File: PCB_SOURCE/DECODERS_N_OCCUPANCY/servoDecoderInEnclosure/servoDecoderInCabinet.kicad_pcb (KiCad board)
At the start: 2 copper layers, 75 x 84 mm, 110 parts, among them J101 Screw_Terminal_01x04, J201 ICSP, J702 USB_B_Mini, U1001 6N137, U202 ATmega328-A, U301 L78L05_SOT89, U701 CH340G, Y201 Crystal_GND2, Y701 Crystal

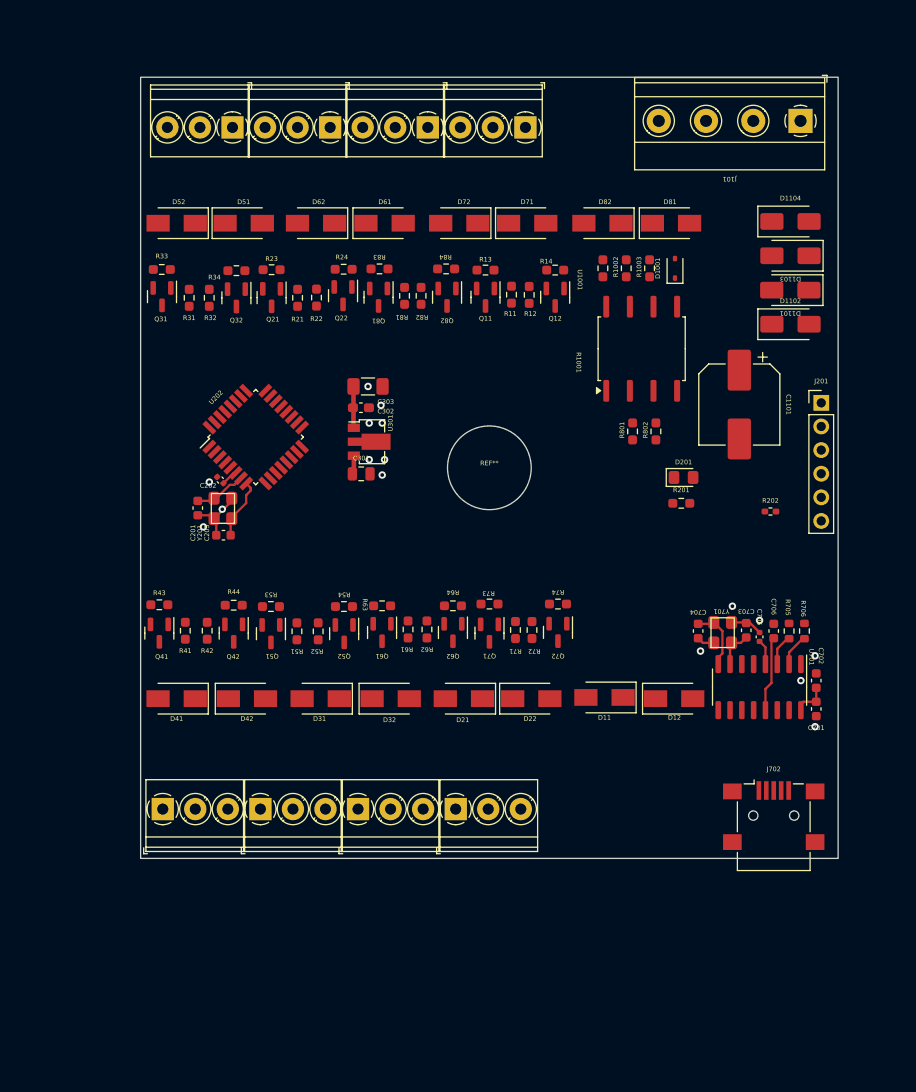
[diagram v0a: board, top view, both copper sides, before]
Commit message: added some boards, new turning loop module with sleeper, all eating LED as well as servoDecoderInEnclosure
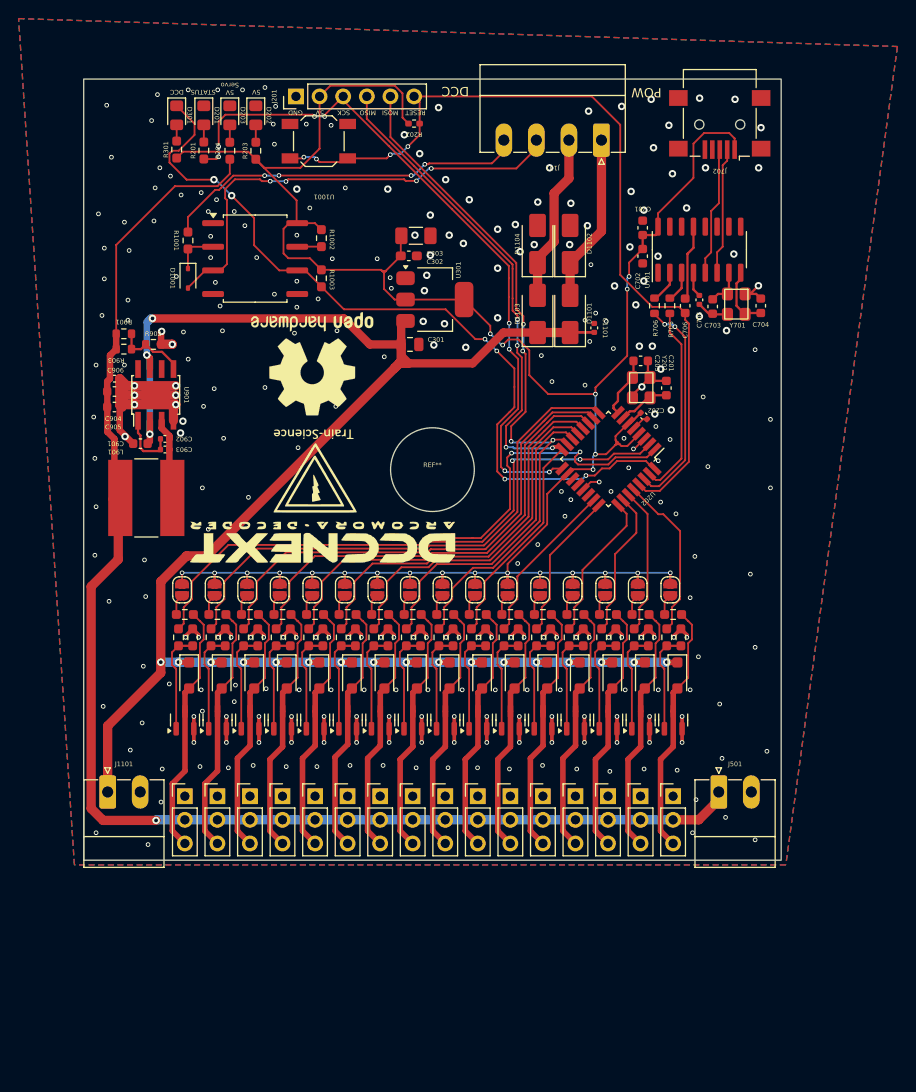
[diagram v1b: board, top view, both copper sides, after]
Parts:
- removed D11, D12, D21, D22, D31, D32, D41, D42, D51, D52, D61, D62, D71, D72, D81, D82: ~, Diode_SMD:D_SMA
- removed Q11, Q12, Q21, Q22, Q31, Q32, Q41, Q42, Q51, Q52, Q61, Q62, Q71, Q72, Q81, Q82: ~, Package_TO_SOT_SMD:SOT-23
- removed R11, R12, R13, R14, R21, R22, R23, R24, R31, R32, R33, R34, R41, R42, R43, R44, R51, R52, R53, R54, R61, R62, R63, R64, R71, R72, R73, R74, R81, R82, R83, R84: ~, Resistor_SMD:R_0603_1608Metric_Pad0.98x0.95mm_HandSolder
- removed the REF** at (218.0, 46.2)
- removed the REF** at (197.0, 46.2)
- removed the REF** at (210.5, 119.5)
- removed the REF** at (207.5, 46.2)
- removed the REF** at (189.5, 119.5)
- removed the REF** at (200.0, 119.5)
- removed the REF** at (186.5, 46.2)
- removed the REF** at (179.0, 119.5)
- added C901: 22uF, Capacitor_SMD:C_0603_1608Metric, F.Cu at (176.6, 80.2)
- added C902: 100nF, Capacitor_SMD:C_0402_1005Metric, F.Cu at (179.2, 79.7)
- added C903: 22nF, Capacitor_SMD:C_0402_1005Metric, F.Cu at (179.2, 80.8)
- added C904: 22uF, Capacitor_SMD:C_0603_1608Metric, F.Cu at (173.8, 74.6)
- added C905: 22uF, Capacitor_SMD:C_0603_1608Metric, F.Cu at (173.8, 76.3)
- added C906: 100nF, Capacitor_SMD:C_0402_1005Metric, F.Cu at (173.8, 73.2)
- added D1002: SM4007, Diode_SMD:D_SOD-123F, F.Cu at (195.8, 105.1)
- added D1301: SM4007, Diode_SMD:D_SOD-123F, F.Cu at (199.3, 105.1)
- added D1401: SM4007, Diode_SMD:D_SOD-123F, F.Cu at (202.8, 105.1)
- added D1501: SM4007, Diode_SMD:D_SOD-123F, F.Cu at (206.3, 105.1)
- added D1601: SM4007, Diode_SMD:D_SOD-123F, F.Cu at (209.8, 105.1)
- added D1701: SM4007, Diode_SMD:D_SOD-123F, F.Cu at (213.3, 105.1)
- added D1801: SM4007, Diode_SMD:D_SOD-123F, F.Cu at (216.8, 105.1)
- added D1901: SM4007, Diode_SMD:D_SOD-123F, F.Cu at (220.3, 105.1)
- added D2001: SM4007, Diode_SMD:D_SOD-123F, F.Cu at (223.8, 105.1)
- added D202: LED, LED_SMD:LED_0805_2012Metric_Pad1.15x1.40mm_HandSolder, F.Cu at (189.0, 44.9)
- added D203: LED, LED_SMD:LED_0805_2012Metric_Pad1.15x1.40mm_HandSolder, F.Cu at (186.2, 44.9)
- added D2101: SM4007, Diode_SMD:D_SOD-123F, F.Cu at (227.3, 105.1)
- added D2201: SM4007, Diode_SMD:D_SOD-123F, F.Cu at (230.8, 105.1)
- added D2301: SM4007, Diode_SMD:D_SOD-123F, F.Cu at (234.3, 105.1)
- added D301: LED, LED_SMD:LED_0805_2012Metric_Pad1.15x1.40mm_HandSolder, F.Cu at (180.5, 44.9)
- added D601: SM4007, Diode_SMD:D_SOD-123F, F.Cu at (185.3, 105.1)
- added D701: SM4007, Diode_SMD:D_SOD-123F, F.Cu at (188.8, 105.1)
- added D801: SM4007, Diode_SMD:D_SOD-123F, F.Cu at (181.8, 105.1)
- added D901: SM4007, Diode_SMD:D_SOD-123F, F.Cu at (192.3, 105.1)
- added G***: LOGO, custom_kicad_lib_sk:Train-Science logo small, F.Cu at (195.3, 83.1)
- added G***: LOGO, custom_kicad_lib_sk:DCC_NEXT_LOGO, F.Cu at (196.2, 90.6)
- added J1001: Conn_01x03_Pin, Connector_PinHeader_2.54mm:PinHeader_1x03_P2.54mm_Vertical, F.Cu at (195.4, 118.1)
- added J1101: Screw_Terminal_01x02, Connector_Phoenix_MC:PhoenixContact_MC_1,5_2-G-3.5_1x02_P3.50mm_Horizontal, F.Cu at (173.1, 117.7)
- added J1301: Conn_01x03_Pin, Connector_PinHeader_2.54mm:PinHeader_1x03_P2.54mm_Vertical, F.Cu at (198.9, 118.1)
- added J1401: Conn_01x03_Pin, Connector_PinHeader_2.54mm:PinHeader_1x03_P2.54mm_Vertical, F.Cu at (202.4, 118.1)
- added J1501: Conn_01x03_Pin, Connector_PinHeader_2.54mm:PinHeader_1x03_P2.54mm_Vertical, F.Cu at (205.9, 118.1)
- added J1601: Conn_01x03_Pin, Connector_PinHeader_2.54mm:PinHeader_1x03_P2.54mm_Vertical, F.Cu at (209.4, 118.1)
- added J1701: Conn_01x03_Pin, Connector_PinHeader_2.54mm:PinHeader_1x03_P2.54mm_Vertical, F.Cu at (212.9, 118.1)
- added J1801: Conn_01x03_Pin, Connector_PinHeader_2.54mm:PinHeader_1x03_P2.54mm_Vertical, F.Cu at (216.4, 118.1)
- added J1901: Conn_01x03_Pin, Connector_PinHeader_2.54mm:PinHeader_1x03_P2.54mm_Vertical, F.Cu at (219.9, 118.1)
- added J2001: Conn_01x03_Pin, Connector_PinHeader_2.54mm:PinHeader_1x03_P2.54mm_Vertical, F.Cu at (223.4, 118.1)
- added J2101: Conn_01x03_Pin, Connector_PinHeader_2.54mm:PinHeader_1x03_P2.54mm_Vertical, F.Cu at (226.9, 118.1)
- added J2201: Conn_01x03_Pin, Connector_PinHeader_2.54mm:PinHeader_1x03_P2.54mm_Vertical, F.Cu at (230.4, 118.1)
- added J2301: Conn_01x03_Pin, Connector_PinHeader_2.54mm:PinHeader_1x03_P2.54mm_Vertical, F.Cu at (233.9, 118.1)
- added J501: Screw_Terminal_01x02, Connector_Phoenix_MC:PhoenixContact_MC_1,5_2-G-3.5_1x02_P3.50mm_Horizontal, F.Cu at (238.8, 117.7)
- added J601: Conn_01x03_Pin, Connector_PinHeader_2.54mm:PinHeader_1x03_P2.54mm_Vertical, F.Cu at (184.9, 118.1)
- added J701: Conn_01x03_Pin, Connector_PinHeader_2.54mm:PinHeader_1x03_P2.54mm_Vertical, F.Cu at (188.4, 118.1)
- added J801: Conn_01x03_Pin, Connector_PinHeader_2.54mm:PinHeader_1x03_P2.54mm_Vertical, F.Cu at (181.4, 118.1)
- added J901: Conn_01x03_Pin, Connector_PinHeader_2.54mm:PinHeader_1x03_P2.54mm_Vertical, F.Cu at (191.9, 118.1)
- added JP1001: SolderJumper_2_Open, Jumper:SolderJumper-2_P1.3mm_Open_RoundedPad1.0x1.5mm, F.Cu at (195.1, 95.9)
- added JP1301: SolderJumper_2_Open, Jumper:SolderJumper-2_P1.3mm_Open_RoundedPad1.0x1.5mm, F.Cu at (198.6, 95.9)
- added JP1401: SolderJumper_2_Open, Jumper:SolderJumper-2_P1.3mm_Open_RoundedPad1.0x1.5mm, F.Cu at (202.1, 95.9)
- added JP1501: SolderJumper_2_Open, Jumper:SolderJumper-2_P1.3mm_Open_RoundedPad1.0x1.5mm, F.Cu at (205.6, 95.9)
- added JP1601: SolderJumper_2_Open, Jumper:SolderJumper-2_P1.3mm_Open_RoundedPad1.0x1.5mm, F.Cu at (209.1, 95.9)
- added JP1701: SolderJumper_2_Open, Jumper:SolderJumper-2_P1.3mm_Open_RoundedPad1.0x1.5mm, F.Cu at (212.6, 95.9)
- added JP1801: SolderJumper_2_Open, Jumper:SolderJumper-2_P1.3mm_Open_RoundedPad1.0x1.5mm, F.Cu at (216.1, 95.9)
- added JP1901: SolderJumper_2_Open, Jumper:SolderJumper-2_P1.3mm_Open_RoundedPad1.0x1.5mm, F.Cu at (219.6, 95.9)
- added JP2001: SolderJumper_2_Open, Jumper:SolderJumper-2_P1.3mm_Open_RoundedPad1.0x1.5mm, F.Cu at (223.1, 95.9)
- added JP2101: SolderJumper_2_Open, Jumper:SolderJumper-2_P1.3mm_Open_RoundedPad1.0x1.5mm, F.Cu at (226.6, 95.9)
- added JP2201: SolderJumper_2_Open, Jumper:SolderJumper-2_P1.3mm_Open_RoundedPad1.0x1.5mm, F.Cu at (230.1, 95.9)
- added JP2301: SolderJumper_2_Open, Jumper:SolderJumper-2_P1.3mm_Open_RoundedPad1.0x1.5mm, F.Cu at (233.6, 95.9)
- added JP601: SolderJumper_2_Open, Jumper:SolderJumper-2_P1.3mm_Open_RoundedPad1.0x1.5mm, F.Cu at (184.6, 95.9)
- added JP701: SolderJumper_2_Open, Jumper:SolderJumper-2_P1.3mm_Open_RoundedPad1.0x1.5mm, F.Cu at (188.1, 95.9)
- added JP801: SolderJumper_2_Open, Jumper:SolderJumper-2_P1.3mm_Open_RoundedPad1.0x1.5mm, F.Cu at (181.1, 95.9)
- added JP901: SolderJumper_2_Open, Jumper:SolderJumper-2_P1.3mm_Open_RoundedPad1.0x1.5mm, F.Cu at (191.6, 95.9)
- added L901: L, Inductor_SMD:L_Bourns-SRN8040_8x8.15mm, F.Cu at (177.2, 86.0)
- added Q1001: AO3400A, Package_TO_SOT_SMD:SOT-23, F.Cu at (195.4, 109.9)
- added Q1301: AO3400A, Package_TO_SOT_SMD:SOT-23, F.Cu at (198.9, 109.9)
- added Q1401: AO3400A, Package_TO_SOT_SMD:SOT-23, F.Cu at (202.4, 109.9)
- added Q1501: AO3400A, Package_TO_SOT_SMD:SOT-23, F.Cu at (205.9, 109.9)
- added Q1601: AO3400A, Package_TO_SOT_SMD:SOT-23, F.Cu at (209.4, 109.9)
- added Q1701: AO3400A, Package_TO_SOT_SMD:SOT-23, F.Cu at (212.9, 109.9)
- added Q1801: AO3400A, Package_TO_SOT_SMD:SOT-23, F.Cu at (216.4, 109.9)
- added Q1901: AO3400A, Package_TO_SOT_SMD:SOT-23, F.Cu at (219.9, 109.9)
- added Q2001: AO3400A, Package_TO_SOT_SMD:SOT-23, F.Cu at (223.4, 109.9)
- added Q2101: AO3400A, Package_TO_SOT_SMD:SOT-23, F.Cu at (226.9, 109.9)
- added Q2201: AO3400A, Package_TO_SOT_SMD:SOT-23, F.Cu at (230.4, 109.9)
- added Q2301: AO3400A, Package_TO_SOT_SMD:SOT-23, F.Cu at (233.9, 109.9)
- added Q601: AO3400A, Package_TO_SOT_SMD:SOT-23, F.Cu at (184.9, 109.9)
- added Q701: AO3400A, Package_TO_SOT_SMD:SOT-23, F.Cu at (188.4, 109.9)
- added Q801: AO3400A, Package_TO_SOT_SMD:SOT-23, F.Cu at (181.4, 109.9)
- added Q901: AO3400A, Package_TO_SOT_SMD:SOT-23, F.Cu at (191.9, 109.9)
- added R1004: 22R, custom_kicad_lib_sk:R_0603_smalltext, F.Cu at (194.7, 101.0)
- added R1005: 22k, custom_kicad_lib_sk:R_0603_smalltext, F.Cu at (196.2, 101.0)
- added R1006: 10k, custom_kicad_lib_sk:R_0603_smalltext, F.Cu at (195.4, 98.6)
- added R1301: 22R, custom_kicad_lib_sk:R_0603_smalltext, F.Cu at (198.2, 101.0)
- added R1302: 22k, custom_kicad_lib_sk:R_0603_smalltext, F.Cu at (199.7, 101.0)
- added R1303: 10k, custom_kicad_lib_sk:R_0603_smalltext, F.Cu at (198.9, 98.6)
- added R1401: 22R, custom_kicad_lib_sk:R_0603_smalltext, F.Cu at (201.7, 101.0)
- added R1402: 22k, custom_kicad_lib_sk:R_0603_smalltext, F.Cu at (203.2, 101.0)
- added R1403: 10k, custom_kicad_lib_sk:R_0603_smalltext, F.Cu at (202.4, 98.6)
- added R1501: 22R, custom_kicad_lib_sk:R_0603_smalltext, F.Cu at (205.2, 101.0)
- added R1502: 22k, custom_kicad_lib_sk:R_0603_smalltext, F.Cu at (206.7, 101.0)
- added R1503: 10k, custom_kicad_lib_sk:R_0603_smalltext, F.Cu at (205.9, 98.6)
- added R1601: 22R, custom_kicad_lib_sk:R_0603_smalltext, F.Cu at (208.7, 101.0)
- added R1602: 22k, custom_kicad_lib_sk:R_0603_smalltext, F.Cu at (210.2, 101.0)
- added R1603: 10k, custom_kicad_lib_sk:R_0603_smalltext, F.Cu at (209.4, 98.6)
- added R1701: 22R, custom_kicad_lib_sk:R_0603_smalltext, F.Cu at (212.2, 101.0)
- added R1702: 22k, custom_kicad_lib_sk:R_0603_smalltext, F.Cu at (213.7, 101.0)
- added R1703: 10k, custom_kicad_lib_sk:R_0603_smalltext, F.Cu at (212.9, 98.6)
- added R1801: 22R, custom_kicad_lib_sk:R_0603_smalltext, F.Cu at (215.7, 101.0)
- added R1802: 22k, custom_kicad_lib_sk:R_0603_smalltext, F.Cu at (217.2, 101.0)
- added R1803: 10k, custom_kicad_lib_sk:R_0603_smalltext, F.Cu at (216.4, 98.6)
- added R1901: 22R, custom_kicad_lib_sk:R_0603_smalltext, F.Cu at (219.2, 101.0)
- added R1902: 22k, custom_kicad_lib_sk:R_0603_smalltext, F.Cu at (220.7, 101.0)
- added R1903: 10k, custom_kicad_lib_sk:R_0603_smalltext, F.Cu at (219.9, 98.6)
- added R2001: 22R, custom_kicad_lib_sk:R_0603_smalltext, F.Cu at (222.7, 101.0)
- added R2002: 22k, custom_kicad_lib_sk:R_0603_smalltext, F.Cu at (224.2, 101.0)
- added R2003: 10k, custom_kicad_lib_sk:R_0603_smalltext, F.Cu at (223.4, 98.6)
- added R203: 6k2, Resistor_SMD:R_0603_1608Metric_Pad0.98x0.95mm_HandSolder, F.Cu at (189.0, 48.7)
- added R204: 6k2, Resistor_SMD:R_0603_1608Metric_Pad0.98x0.95mm_HandSolder, F.Cu at (186.2, 48.7)
- added R2101: 22R, custom_kicad_lib_sk:R_0603_smalltext, F.Cu at (226.2, 101.0)
- added R2102: 22k, custom_kicad_lib_sk:R_0603_smalltext, F.Cu at (227.7, 101.0)
- added R2103: 10k, custom_kicad_lib_sk:R_0603_smalltext, F.Cu at (226.9, 98.6)
- added R2201: 22R, custom_kicad_lib_sk:R_0603_smalltext, F.Cu at (229.7, 101.0)
- added R2202: 22k, custom_kicad_lib_sk:R_0603_smalltext, F.Cu at (231.2, 101.0)
- added R2203: 10k, custom_kicad_lib_sk:R_0603_smalltext, F.Cu at (230.4, 98.6)
- added R2301: 22R, custom_kicad_lib_sk:R_0603_smalltext, F.Cu at (233.2, 101.0)
- added R2302: 22k, custom_kicad_lib_sk:R_0603_smalltext, F.Cu at (234.7, 101.0)
- added R2303: 10k, custom_kicad_lib_sk:R_0603_smalltext, F.Cu at (233.9, 98.6)
- added R301: 6k2, Resistor_SMD:R_0603_1608Metric_Pad0.98x0.95mm_HandSolder, F.Cu at (180.5, 48.6)
- added R601: 22R, custom_kicad_lib_sk:R_0603_smalltext, F.Cu at (184.2, 101.0)
- added R602: 22k, custom_kicad_lib_sk:R_0603_smalltext, F.Cu at (185.7, 101.0)
- added R603: 10k, custom_kicad_lib_sk:R_0603_smalltext, F.Cu at (184.9, 98.6)
- added R701: 22R, custom_kicad_lib_sk:R_0603_smalltext, F.Cu at (187.7, 101.0)
- added R702: 22k, custom_kicad_lib_sk:R_0603_smalltext, F.Cu at (189.2, 101.0)
- added R703: 10k, custom_kicad_lib_sk:R_0603_smalltext, F.Cu at (188.4, 98.6)
- added R803: 10k, custom_kicad_lib_sk:R_0603_smalltext, F.Cu at (181.4, 98.6)
- added R901: 220k, Resistor_SMD:R_0603_1608Metric, F.Cu at (174.8, 68.4)
- added R902: 20k, Resistor_SMD:R_0603_1608Metric, F.Cu at (178.0, 69.5)
- added R903: 150k, Resistor_SMD:R_0603_1608Metric, F.Cu at (174.8, 70.0)
- added R904: 22R, custom_kicad_lib_sk:R_0603_smalltext, F.Cu at (191.2, 101.0)
- added R905: 22k, custom_kicad_lib_sk:R_0603_smalltext, F.Cu at (192.7, 101.0)
- added R906: 10k, custom_kicad_lib_sk:R_0603_smalltext, F.Cu at (191.9, 98.6)
- added REF**: OSHW-Logo2_14.6x12mm_SilkScreen, Symbol:OSHW-Logo2_14.6x12mm_SilkScreen, F.Cu at (195.1, 71.6)
- added SW201: default_switch, custom_kicad_lib_sk:default_switch, F.Cu at (195.8, 47.7)
- added U901: MT2499A, Package_SO:TI_SO-PowerPAD-8, F.Cu at (178.2, 75.0)
- C1101: value 1000uF -> 100nF; footprint Capacitor_SMD:CP_Elec_8x10.5 -> Capacitor_SMD:C_0402_1005Metric
- J101: value Screw_Terminal_01x04 -> FEMALE; footprint TerminalBlock_Phoenix:TerminalBlock_Phoenix_MKDS-1,5-4-5.08_1x04_P5.08mm_Horizontal -> Connector_Phoenix_MC:PhoenixContact_MC_1,5_4-G-3.5_1x04_P3.50mm_Horizontal
- R801: value 10k -> 22R
- R802: value 10k -> 22k
- U301: value L78L05_SOT89 -> AMS1117-5.0; footprint Package_TO_SOT_SMD:SOT-89-3 -> Package_TO_SOT_SMD:SOT-223-3_TabPin2
- moved J702 74.5 mm to (238.9, 45.9), turned to 180 degrees
- moved J201 65.4 mm to (193.3, 42.9), turned to 90 degrees
- moved D201 64.6 mm to (183.4, 44.9), turned to -90 degrees
- moved R201 63.8 mm to (183.4, 48.7), turned to 90 degrees
- moved R202 56.6 mm to (206.0, 45.8), turned to 180 degrees
- moved C701 55.0 mm to (230.6, 57.0), turned to 90 degrees
- moved R802 54.5 mm to (182.2, 101.0)
- moved R801 53.6 mm to (180.7, 101.0), turned to -90 degrees
- moved D1001 52.4 mm to (181.7, 62.4), turned to -90 degrees
- moved C201 52.0 mm to (233.2, 74.2), turned to -90 degrees
- moved C702 49.3 mm to (230.6, 60.0), turned to -90 degrees
- moved C203 48.6 mm to (230.4, 71.3), turned to 180 degrees
- moved U701 47.5 mm to (236.7, 59.3), turned to 90 degrees
- moved Y201 46.4 mm to (230.2, 74.1), turned to 90 degrees
- moved C202 46.1 mm to (230.7, 77.2), turned to -45 degrees
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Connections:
- net /A renamed /DCC/A
- net /B renamed /DCC/B
- net /atmega/sw3 renamed /atmega/P9
- net /atmega/sw4 renamed /atmega/P10
- C1101 pad 1: /Buck/VCC -> GND
- C1101 pad 2: GND -> VCC
- C301 pad 1: /Buck/VCC -> VCC
- D1101 pad 1: /Buck/VCC -> VCC
- D1101 pad 2: /D_bridge/AC_1 -> /D_bridge/AC_2
- D1102 pad 1: /D_bridge/AC_1 -> /D_bridge/AC_2
- D1103 pad 1: /Buck/VCC -> VCC
- D1103 pad 2: /D_bridge/AC_2 -> /D_bridge/AC_1
- D1104 pad 1: /D_bridge/AC_2 -> /D_bridge/AC_1
- D201 pad 1: /atmega/LED -> GND
- R201 pad 1: +5V -> /atmega/LED
- R801 pad 1: /atmega/bus2.pin1 -> /atmega/P1
- R801 pad 2: +5V -> Net-(Q801-G)
- R802 pad 1: /atmega/bus2.pin2 -> Net-(Q801-G)
- R802 pad 2: +5V -> GND
- U202 pad 1: /atmega/bus1.pin1 -> /atmega/P1
- U202 pad 10: /atmega/bus1.relay2 -> /atmega/P4
- U202 pad 11: /atmega/bus2.pin1 -> /atmega/P5
- U202 pad 12: /atmega/bus2.relay1 -> /atmega/P6
- U202 pad 13: /atmega/sw1 -> /atmega/P7
- U202 pad 14: /atmega/sw2 -> /atmega/P8
- U202 pad 2: /atmega/bus1.pin2 -> /atmega/P2
- U202 pad 23: /atmega/bus2.relay2 -> /atmega/P11
- U202 pad 24: /atmega/bus2.pin2 -> /atmega/P12
- U202 pad 25: /atmega/bus3.pin1 -> /atmega/P13
- U202 pad 26: /atmega/bus3.pin2 -> /atmega/P14
- U202 pad 27: /atmega/bus3.relay1 -> /atmega/P15
- U202 pad 28: /atmega/bus3.relay2 -> /atmega/P16
- U202 pad 9: /atmega/bus1.relay1 -> /atmega/P3
- U301 pad 1: +5V -> GND
- U301 pad 2: GND -> +5V
- U301 pad 3: /Buck/VCC -> VCC
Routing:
- net VCC: track 0.00 -> 262.1 mm, vias 0 -> 20
- net +5V: track 10.1 -> 266.1 mm, vias 0 -> 23
- net +5VA: track 0.00 -> 149.6 mm, vias 0 -> 1
- net GND: track 12.2 -> 134.1 mm, vias 11 -> 288
- net /USB/Reset: track 0.00 -> 91.3 mm, vias 0 -> 4
- net /DCC/DCC_TTL: track 0.00 -> 87.0 mm, vias 0 -> 6
- net /atmega/P9: track 0.00 -> 76.9 mm, vias 0 -> 4
- net /atmega/P10: track 0.00 -> 76.1 mm, vias 0 -> 4
- net /atmega/LED: track 0.00 -> 75.6 mm, vias 0 -> 8
- net /atmega/P1: track 0.00 -> 67.5 mm, vias 0 -> 2
- net /atmega/P2: track 0.00 -> 60.9 mm, vias 0 -> 2
- net /atmega/P3: track 0.00 -> 54.8 mm
- net /atmega/P4: track 0.00 -> 50.6 mm
- net /DCC/B: track 0.00 -> 49.9 mm, vias 0 -> 4
- net /atmega/P5: track 0.00 -> 46.4 mm
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- added copper zone on B.Cu, net GND
- added copper zone on F.Cu, net GND
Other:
- board text added: "5V"
- board text added: "5V Servo"
- board text added: "DCC"
- board text added: "GND"
- board text added: "MISO"
- board text added: "MOSI"
- board text added: "POW"
- board text added: "RESET"
- board text added: "SCK"
- board text added: "STATUS"

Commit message: added S88 current sense to releases and update OSSD decoder
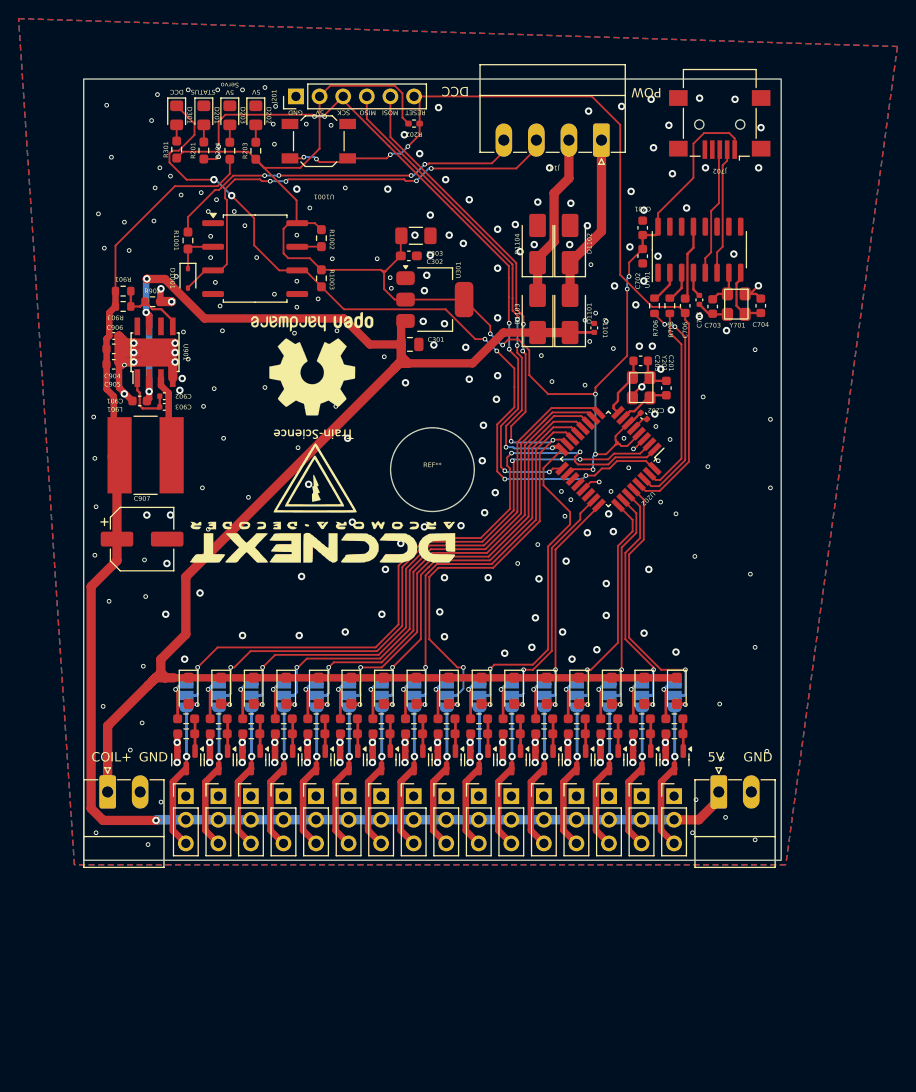
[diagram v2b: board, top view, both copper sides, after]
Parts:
- removed D1002, D1301, D1401, D1501, D1601, D1701, D1801, D1901, D2001, D2201, D2301, D601, D701, D801, D901: SM4007, Diode_SMD:D_SOD-123F
- removed J1001, J1301, J1401, J1501, J1601, J1701, J1801, J1901, J2001, J2201, J2301, J601, J701, J801, J901: Conn_01x03_Pin, Connector_PinHeader_2.54mm:PinHeader_1x03_P2.54mm_Vertical
- removed JP1001, JP1301, JP1401, JP1501, JP1601, JP1701, JP1801, JP1901, JP2001, JP2201, JP2301, JP601, JP701, JP801, JP901: SolderJumper_2_Open, Jumper:SolderJumper-2_P1.3mm_Open_RoundedPad1.0x1.5mm
- removed Q1001, Q1301, Q1401, Q1501, Q1601, Q1701, Q1801, Q1901, Q2001, Q2201, Q2301, Q601, Q701, Q801, Q901: AO3400A, Package_TO_SOT_SMD:SOT-23
- removed R1004, R1301, R1401, R1501, R1601, R1701, R1801, R1901, R2001, R2201, R2301, R601, R701, R801, R904: 22R, custom_kicad_lib_sk:R_0603_smalltext
- removed R1005, R1302, R1402, R1502, R1602, R1702, R1802, R1902, R2002, R2202, R2302, R602, R702, R802, R905: 22k, custom_kicad_lib_sk:R_0603_smalltext
- removed R1006, R1303, R1403, R1503, R1603, R1703, R1803, R1903, R2003, R2103, R603, R703, R803, R906: 10k, custom_kicad_lib_sk:R_0603_smalltext
- added C907: 470uF, Capacitor_SMD:CP_Elec_6.3x7.7, F.Cu at (176.8, 90.5)
- added D2202: SM4007, Diode_SMD:D_SOD-123F, F.Cu at (185.3, 106.8)
- added D2302: SM4007, Diode_SMD:D_SOD-123F, F.Cu at (188.8, 106.8)
- added D2401: SM4007, Diode_SMD:D_SOD-123F, F.Cu at (192.3, 106.8)
- added D2501: SM4007, Diode_SMD:D_SOD-123F, F.Cu at (195.8, 106.8)
- added D2601: SM4007, Diode_SMD:D_SOD-123F, F.Cu at (199.3, 106.8)
- added D2701: SM4007, Diode_SMD:D_SOD-123F, F.Cu at (202.8, 106.8)
- added D2801: SM4007, Diode_SMD:D_SOD-123F, F.Cu at (206.3, 106.8)
- added D2901: SM4007, Diode_SMD:D_SOD-123F, F.Cu at (209.8, 106.8)
- added D3001: SM4007, Diode_SMD:D_SOD-123F, F.Cu at (213.3, 106.8)
- added D3101: SM4007, Diode_SMD:D_SOD-123F, F.Cu at (216.8, 106.8)
- added D3201: SM4007, Diode_SMD:D_SOD-123F, F.Cu at (220.3, 106.8)
- added D3301: SM4007, Diode_SMD:D_SOD-123F, F.Cu at (223.8, 106.8)
- added D3401: SM4007, Diode_SMD:D_SOD-123F, F.Cu at (227.3, 106.8)
- added D3501: SM4007, Diode_SMD:D_SOD-123F, F.Cu at (230.8, 106.8)
- added D3601: SM4007, Diode_SMD:D_SOD-123F, F.Cu at (234.3, 106.8)
- added J2202: Conn_01x03_Pin, Connector_PinHeader_2.54mm:PinHeader_1x03_P2.54mm_Vertical, F.Cu at (185.0, 118.1)
- added J2302: Conn_01x03_Pin, Connector_PinHeader_2.54mm:PinHeader_1x03_P2.54mm_Vertical, F.Cu at (188.5, 118.1)
- added J2401: Conn_01x03_Pin, Connector_PinHeader_2.54mm:PinHeader_1x03_P2.54mm_Vertical, F.Cu at (192.0, 118.1)
- added J2501: Conn_01x03_Pin, Connector_PinHeader_2.54mm:PinHeader_1x03_P2.54mm_Vertical, F.Cu at (195.5, 118.1)
- added J2601: Conn_01x03_Pin, Connector_PinHeader_2.54mm:PinHeader_1x03_P2.54mm_Vertical, F.Cu at (199.0, 118.1)
- added J2701: Conn_01x03_Pin, Connector_PinHeader_2.54mm:PinHeader_1x03_P2.54mm_Vertical, F.Cu at (202.5, 118.1)
- added J2801: Conn_01x03_Pin, Connector_PinHeader_2.54mm:PinHeader_1x03_P2.54mm_Vertical, F.Cu at (206.0, 118.1)
- added J2901: Conn_01x03_Pin, Connector_PinHeader_2.54mm:PinHeader_1x03_P2.54mm_Vertical, F.Cu at (209.5, 118.1)
- added J3001: Conn_01x03_Pin, Connector_PinHeader_2.54mm:PinHeader_1x03_P2.54mm_Vertical, F.Cu at (213.0, 118.1)
- added J3101: Conn_01x03_Pin, Connector_PinHeader_2.54mm:PinHeader_1x03_P2.54mm_Vertical, F.Cu at (216.5, 118.1)
- added J3201: Conn_01x03_Pin, Connector_PinHeader_2.54mm:PinHeader_1x03_P2.54mm_Vertical, F.Cu at (220.0, 118.1)
- added J3301: Conn_01x03_Pin, Connector_PinHeader_2.54mm:PinHeader_1x03_P2.54mm_Vertical, F.Cu at (223.5, 118.1)
- added J3401: Conn_01x03_Pin, Connector_PinHeader_2.54mm:PinHeader_1x03_P2.54mm_Vertical, F.Cu at (227.0, 118.1)
- added J3501: Conn_01x03_Pin, Connector_PinHeader_2.54mm:PinHeader_1x03_P2.54mm_Vertical, F.Cu at (230.5, 118.1)
- added J3601: Conn_01x03_Pin, Connector_PinHeader_2.54mm:PinHeader_1x03_P2.54mm_Vertical, F.Cu at (234.0, 118.1)
- added JP2202: Jumper_3_Open, Jumper:SolderJumper-3_P1.3mm_Open_RoundedPad1.0x1.5mm, B.Cu at (185.1, 107.3)
- added JP2302: Jumper_3_Open, Jumper:SolderJumper-3_P1.3mm_Open_RoundedPad1.0x1.5mm, B.Cu at (188.6, 107.3)
- added JP2401: Jumper_3_Open, Jumper:SolderJumper-3_P1.3mm_Open_RoundedPad1.0x1.5mm, B.Cu at (192.1, 107.3)
- added JP2501: Jumper_3_Open, Jumper:SolderJumper-3_P1.3mm_Open_RoundedPad1.0x1.5mm, B.Cu at (195.6, 107.3)
- added JP2601: Jumper_3_Open, Jumper:SolderJumper-3_P1.3mm_Open_RoundedPad1.0x1.5mm, B.Cu at (199.1, 107.3)
- added JP2701: Jumper_3_Open, Jumper:SolderJumper-3_P1.3mm_Open_RoundedPad1.0x1.5mm, B.Cu at (202.6, 107.3)
- added JP2801: Jumper_3_Open, Jumper:SolderJumper-3_P1.3mm_Open_RoundedPad1.0x1.5mm, B.Cu at (206.1, 107.3)
- added JP2901: Jumper_3_Open, Jumper:SolderJumper-3_P1.3mm_Open_RoundedPad1.0x1.5mm, B.Cu at (209.6, 107.3)
- added JP3001: Jumper_3_Open, Jumper:SolderJumper-3_P1.3mm_Open_RoundedPad1.0x1.5mm, B.Cu at (213.1, 107.3)
- added JP3101: Jumper_3_Open, Jumper:SolderJumper-3_P1.3mm_Open_RoundedPad1.0x1.5mm, B.Cu at (216.6, 107.3)
- added JP3201: Jumper_3_Open, Jumper:SolderJumper-3_P1.3mm_Open_RoundedPad1.0x1.5mm, B.Cu at (220.1, 107.3)
- added JP3301: Jumper_3_Open, Jumper:SolderJumper-3_P1.3mm_Open_RoundedPad1.0x1.5mm, B.Cu at (223.6, 107.3)
- added JP3401: Jumper_3_Open, Jumper:SolderJumper-3_P1.3mm_Open_RoundedPad1.0x1.5mm, B.Cu at (227.1, 107.3)
- added JP3501: Jumper_3_Open, Jumper:SolderJumper-3_P1.3mm_Open_RoundedPad1.0x1.5mm, B.Cu at (230.6, 107.3)
- added JP3601: Jumper_3_Open, Jumper:SolderJumper-3_P1.3mm_Open_RoundedPad1.0x1.5mm, B.Cu at (234.1, 107.3)
- added Q2202: AO3400A, Package_TO_SOT_SMD:SOT-23, F.Cu at (185.0, 114.2)
- added Q2302: AO3400A, Package_TO_SOT_SMD:SOT-23, F.Cu at (188.5, 114.2)
- added Q2401: AO3400A, Package_TO_SOT_SMD:SOT-23, F.Cu at (192.0, 114.2)
- added Q2501: AO3400A, Package_TO_SOT_SMD:SOT-23, F.Cu at (195.5, 114.2)
- added Q2601: AO3400A, Package_TO_SOT_SMD:SOT-23, F.Cu at (199.0, 114.2)
- added Q2701: AO3400A, Package_TO_SOT_SMD:SOT-23, F.Cu at (202.5, 114.2)
- added Q2801: AO3400A, Package_TO_SOT_SMD:SOT-23, F.Cu at (206.0, 114.2)
- added Q2901: AO3400A, Package_TO_SOT_SMD:SOT-23, F.Cu at (209.5, 114.2)
- added Q3001: AO3400A, Package_TO_SOT_SMD:SOT-23, F.Cu at (213.0, 114.2)
- added Q3101: AO3400A, Package_TO_SOT_SMD:SOT-23, F.Cu at (216.5, 114.2)
- added Q3201: AO3400A, Package_TO_SOT_SMD:SOT-23, F.Cu at (220.0, 114.2)
- added Q3301: AO3400A, Package_TO_SOT_SMD:SOT-23, F.Cu at (223.5, 114.2)
- added Q3401: AO3400A, Package_TO_SOT_SMD:SOT-23, F.Cu at (227.0, 114.2)
- added Q3501: AO3400A, Package_TO_SOT_SMD:SOT-23, F.Cu at (230.5, 114.2)
- added Q3601: AO3400A, Package_TO_SOT_SMD:SOT-23, F.Cu at (234.0, 114.2)
- added R2204: 22k, custom_kicad_lib_sk:R_0603_smalltext, F.Cu at (185.0, 111.4)
- added R2304: 22k, custom_kicad_lib_sk:R_0603_smalltext, F.Cu at (188.5, 111.4)
- added R2401: 22R, custom_kicad_lib_sk:R_0603_smalltext, F.Cu at (192.0, 109.8)
- added R2402: 22k, custom_kicad_lib_sk:R_0603_smalltext, F.Cu at (192.0, 111.4)
- added R2501: 22R, custom_kicad_lib_sk:R_0603_smalltext, F.Cu at (195.5, 109.8)
- added R2502: 22k, custom_kicad_lib_sk:R_0603_smalltext, F.Cu at (195.5, 111.4)
- added R2601: 22R, custom_kicad_lib_sk:R_0603_smalltext, F.Cu at (199.0, 109.8)
- added R2602: 22k, custom_kicad_lib_sk:R_0603_smalltext, F.Cu at (199.0, 111.4)
- added R2701: 22R, custom_kicad_lib_sk:R_0603_smalltext, F.Cu at (202.5, 109.8)
- added R2702: 22k, custom_kicad_lib_sk:R_0603_smalltext, F.Cu at (202.5, 111.4)
- added R2801: 22R, custom_kicad_lib_sk:R_0603_smalltext, F.Cu at (206.0, 109.8)
- added R2802: 22k, custom_kicad_lib_sk:R_0603_smalltext, F.Cu at (206.0, 111.4)
- added R2901: 22R, custom_kicad_lib_sk:R_0603_smalltext, F.Cu at (209.5, 109.8)
- added R2902: 22k, custom_kicad_lib_sk:R_0603_smalltext, F.Cu at (209.5, 111.4)
- added R3001: 22R, custom_kicad_lib_sk:R_0603_smalltext, F.Cu at (213.0, 109.8)
- added R3002: 22k, custom_kicad_lib_sk:R_0603_smalltext, F.Cu at (213.0, 111.4)
- added R3101: 22R, custom_kicad_lib_sk:R_0603_smalltext, F.Cu at (216.5, 109.8)
- added R3102: 22k, custom_kicad_lib_sk:R_0603_smalltext, F.Cu at (216.5, 111.4)
- added R3201: 22R, custom_kicad_lib_sk:R_0603_smalltext, F.Cu at (220.0, 109.8)
- added R3202: 22k, custom_kicad_lib_sk:R_0603_smalltext, F.Cu at (220.0, 111.4)
- added R3301: 22R, custom_kicad_lib_sk:R_0603_smalltext, F.Cu at (223.5, 109.8)
- added R3302: 22k, custom_kicad_lib_sk:R_0603_smalltext, F.Cu at (223.5, 111.4)
- added R3401: 22R, custom_kicad_lib_sk:R_0603_smalltext, F.Cu at (227.0, 109.8)
- added R3402: 22k, custom_kicad_lib_sk:R_0603_smalltext, F.Cu at (227.0, 111.4)
- added R3501: 22R, custom_kicad_lib_sk:R_0603_smalltext, F.Cu at (230.5, 109.8)
- added R3502: 22k, custom_kicad_lib_sk:R_0603_smalltext, F.Cu at (230.5, 111.4)
- added R3601: 22R, custom_kicad_lib_sk:R_0603_smalltext, F.Cu at (234.0, 109.8)
- added R3602: 22k, custom_kicad_lib_sk:R_0603_smalltext, F.Cu at (234.0, 111.4)
- D1101, D1102, D1103, D1104: value SS53 -> D
- JP2101: value SolderJumper_2_Open -> Jumper_3_Open; footprint Jumper:SolderJumper-2_P1.3mm_Open_RoundedPad1.0x1.5mm -> Jumper:SolderJumper-3_P1.3mm_Open_RoundedPad1.0x1.5mm; moved to B.Cu
- R2203, R2303: value 10k -> 22R
- moved R2102 47.3 mm to (181.5, 111.4), turned to 180 degrees
- moved R2203 46.7 mm to (185.0, 109.8)
- moved R2303 46.7 mm to (188.5, 109.8)
- moved JP2101 46.4 mm to (181.6, 107.3)
- moved D2101 45.6 mm to (181.8, 106.8)
- moved Q2101 45.6 mm to (181.5, 114.2), turned to -90 degrees
- moved R2101 45.5 mm to (181.5, 109.8), turned to 0 degrees
- moved J2101 45.4 mm to (181.5, 118.1)
- moved C901 4.59 mm to (176.5, 75.6)
- moved C906 4.59 mm to (173.7, 68.6)
- moved C902 4.59 mm to (179.2, 75.1)
- moved C903 4.59 mm to (179.2, 76.2)
- moved C904 4.59 mm to (173.7, 70.0)
- moved C905 4.59 mm to (173.7, 71.7)
- moved L901 4.59 mm to (177.2, 81.5)
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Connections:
- JP2101 pad 1: Net-(JP2101-A) -> Net-(D2101-A)
- JP2101 pad 2: +5V -> /atmega/P1
- R2101 pad 1: /atmega/P14 -> Net-(JP2101-B)
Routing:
- net +5V: track 266.1 -> 161.7 mm, vias 23 -> 7
- net VCC: track 262.1 -> 196.0 mm, vias 20 -> 3
- net GND: track 134.1 -> 100.9 mm, vias 288 -> 260
- net Net-(D901-A): track 27.0 -> 0.00 mm
- net Net-(D701-A): track 27.0 -> 0.00 mm
- net Net-(D601-A): track 27.0 -> 0.00 mm
- net Net-(D1901-A): track 27.0 -> 0.00 mm
- net Net-(D1601-A): track 27.0 -> 0.00 mm
- net Net-(D1002-A): track 27.0 -> 0.00 mm
- net Net-(D801-A): track 27.0 -> 0.00 mm
- net Net-(D2001-A): track 27.0 -> 0.00 mm
- net Net-(D1801-A): track 27.0 -> 0.00 mm
- net Net-(D1701-A): track 27.0 -> 0.00 mm
- net Net-(D1401-A): track 27.0 -> 0.00 mm
- net Net-(D1301-A): track 27.0 -> 0.00 mm
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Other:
- board text added: "COIL+"
- board text added: "Coil power"
- board text added: "Servo / Inputs"
- board text added: "solder these pads for -->"

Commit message: upgraded servo driver code to newest standard
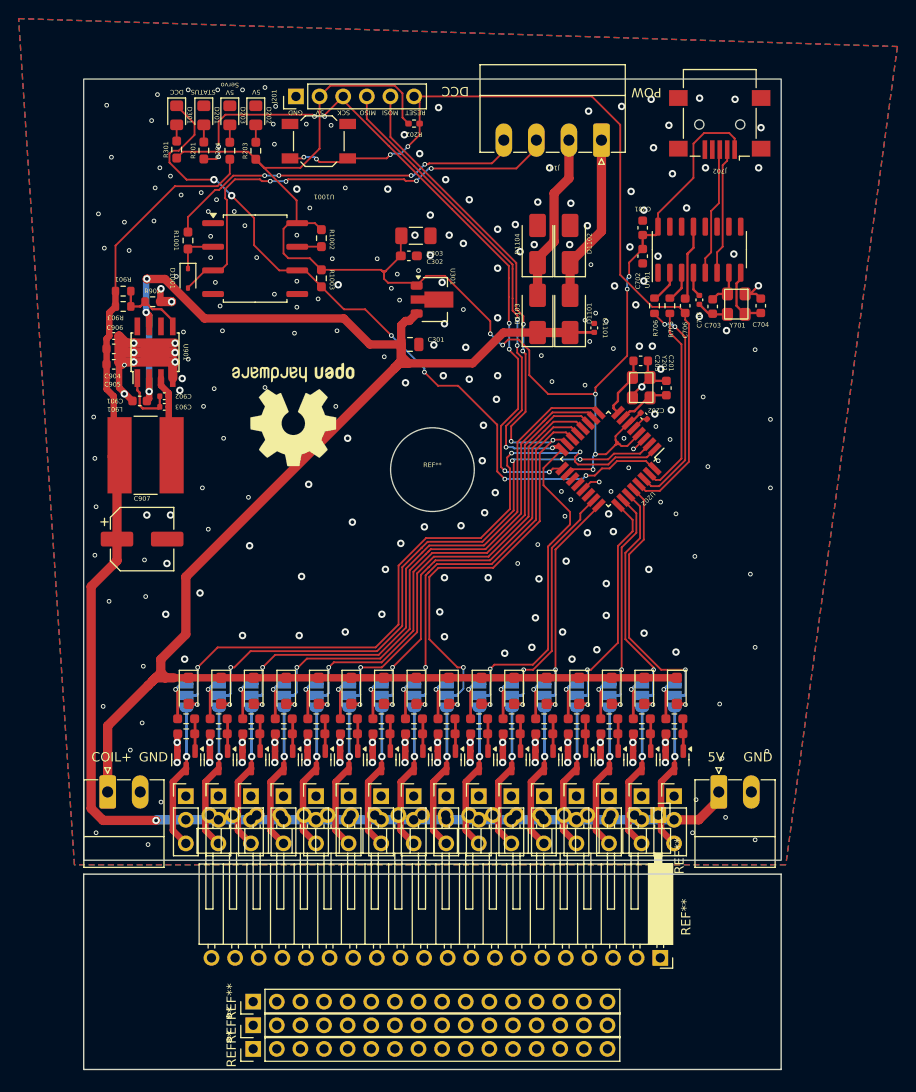
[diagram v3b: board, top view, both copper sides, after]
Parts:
- removed G***: LOGO, custom_kicad_lib_sk:Train-Science logo small
- removed G***: LOGO, custom_kicad_lib_sk:DCC_NEXT_LOGO
- added REF**: PinHeader_1x20_P2.54mm_Horizontal, Connector_PinHeader_2.54mm:PinHeader_1x20_P2.54mm_Horizontal, F.Cu at (232.3, 120.1)
- added REF**: PinHeader_1x16_P2.54mm_Vertical, Connector_PinHeader_2.54mm:PinHeader_1x16_P2.54mm_Vertical, F.Cu at (188.7, 145.3)
- added REF**: PinHeader_1x16_P2.54mm_Vertical, Connector_PinHeader_2.54mm:PinHeader_1x16_P2.54mm_Vertical, F.Cu at (188.7, 140.2)
- added REF**: PinSocket_1x20_P2.54mm_Horizontal, Connector_PinSocket_2.54mm:PinSocket_1x20_P2.54mm_Horizontal, F.Cu at (232.5, 135.5)
- added REF**: PinHeader_1x16_P2.54mm_Vertical, Connector_PinHeader_2.54mm:PinHeader_1x16_P2.54mm_Vertical, F.Cu at (188.7, 142.7)
- U301: value AMS1117-5.0 -> L78L05_SOT89; footprint Package_TO_SOT_SMD:SOT-223-3_TabPin2 -> Package_TO_SOT_SMD:SOT-89-3
- moved REF** 5.83 mm to (193.0, 77.1)
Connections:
- U301 pad 1: GND -> +5V
- U301 pad 2: +5V -> GND
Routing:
- net /DCC/DCC_TTL: track 87.0 -> 80.8 mm
- net VCC: track 196.0 -> 197.6 mm
- net +5V: track 161.7 -> 162.2 mm
- net GND: vias 260 -> 263
